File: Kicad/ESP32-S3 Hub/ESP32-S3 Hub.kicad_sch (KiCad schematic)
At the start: 26 parts, among them U1 ESP32-S3, Y1 ABM11-40.000MHZ-B1U-T3, 10ppm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

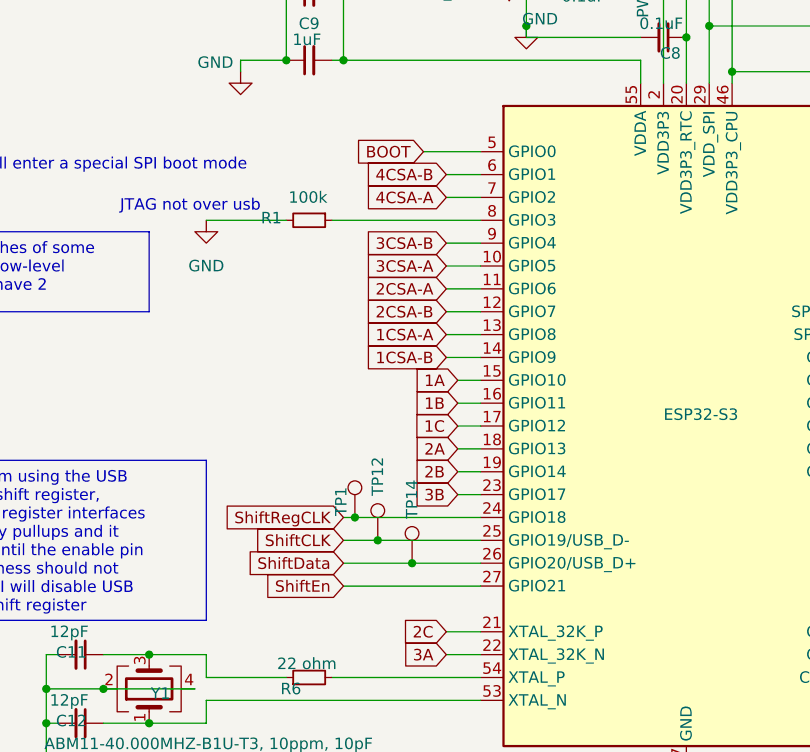
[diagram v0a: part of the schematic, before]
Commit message: Finished basic routing
Now I have to fix some things to try and reduce crosstalk, and improve signal integrity. The likelihood of me being able to completely fix it is low, due to limited space. I also have to run the DRC, and fix the silkscreen.
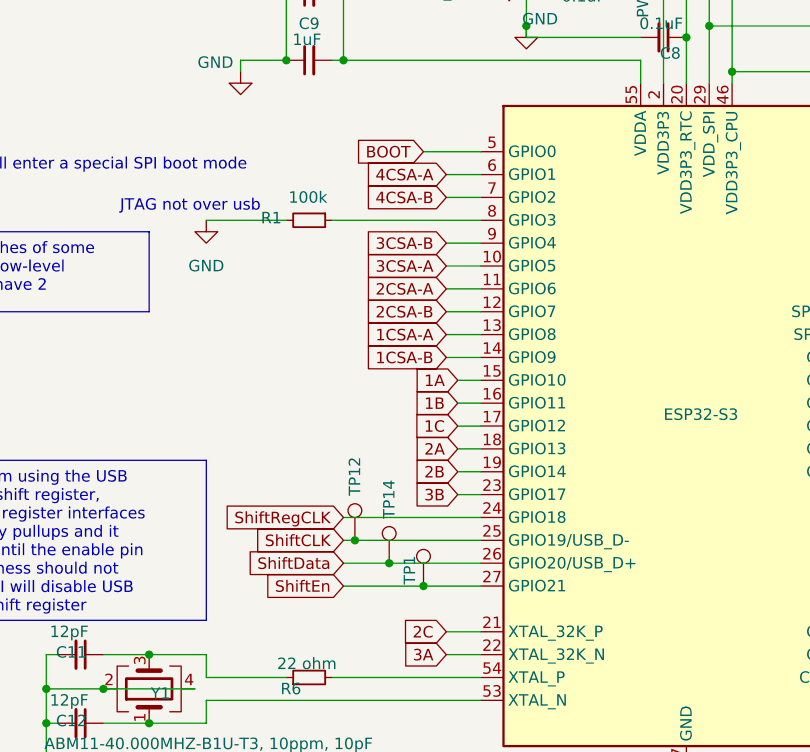
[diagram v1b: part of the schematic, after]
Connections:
- net 4CSA-A: now also U1.6 (GPIO1); no longer U1.7 (GPIO2)
- net 4CSA-B: now also U1.7 (GPIO2); no longer U1.6 (GPIO1)
- net ShiftEn: now also TP1.1
- net ShiftRegCLK: no longer TP1.1
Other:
- moved on the sheet: TP1, TP12, TP14
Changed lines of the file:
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@@
 	)
 	(junction
-		(at 110.49 105.41)
-		(diameter 0)
-		(color 0 0 0 0)
-	)
-	(junction
-		(at 107.95 102.87)
+		(at 111.76 107.95)
 		(diameter 0)
 		(color 0 0 0 0)
@@
 	)
 	(junction
+		(at 107.95 105.41)
+		(diameter 0)
+		(color 0 0 0 0)
+	)
+	(junction
 		(at 142.24 31.75)
 		(diameter 0)
@@
 	)
 	(junction
-		(at 114.3 107.95)
+		(at 115.57 110.49)
 		(diameter 0)
 		(color 0 0 0 0)
@@
 	(wire
 		(pts
-			(xy 107.95 102.87) (xy 121.92 102.87)
-		)
-		(stroke
-			(width 0)
-			(type default)
-		)
-	)
-	(wire
-		(pts
 			(xy 73.66 121.92) (xy 73.66 125.73)
 		)
@@
 	(wire
 		(pts
+			(xy 111.76 107.95) (xy 121.92 107.95)
+		)
+		(stroke
+			(width 0)
+			(type default)
+		)
+	)
+	(wire
+		(pts
 			(xy 176.53 102.87) (xy 180.34 102.87)
 		)
@@
 	(wire
 		(pts
-			(xy 106.68 102.87) (xy 107.95 102.87)
+			(xy 106.68 102.87) (xy 121.92 102.87)
 		)
 		(stroke
@@
 	(wire
 		(pts
-			(xy 110.49 105.41) (xy 121.92 105.41)
-		)
-		(stroke
-			(width 0)
-			(type default)
-		)
-	)
-	(wire
-		(pts
 			(xy 139.7 54.61) (xy 139.7 52.07)
 		)
@@
 	(wire
 		(pts
+			(xy 107.95 105.41) (xy 121.92 105.41)
+		)
+		(stroke
+			(width 0)
+			(type default)
+		)
+	)
+	(wire
+		(pts
 			(xy 85.09 118.11) (xy 91.44 118.11)
 		)
@@
 	(wire
 		(pts
-			(xy 106.68 110.49) (xy 121.92 110.49)
+			(xy 106.68 110.49) (xy 115.57 110.49)
 		)
 		(stroke
@@
 	(wire
 		(pts
-			(xy 106.68 107.95) (xy 114.3 107.95)
+			(xy 106.68 107.95) (xy 111.76 107.95)
 		)
 		(stroke
@@
 	(wire
 		(pts
-			(xy 142.24 40.64) (xy 142.24 44.45)
+			(xy 115.57 110.49) (xy 121.92 110.49)
 		)
 		(stroke
@@
 	(wire
 		(pts
-			(xy 137.16 40.64) (xy 142.24 40.64)
+			(xy 142.24 40.64) (xy 142.24 44.45)
 		)
 		(stroke
@@
 	(wire
 		(pts
-			(xy 118.11 85.09) (xy 121.92 85.09)
+			(xy 137.16 40.64) (xy 142.24 40.64)
 		)
 		(stroke
@@
 	(wire
 		(pts
-			(xy 91.44 125.73) (xy 85.09 125.73)
+			(xy 118.11 85.09) (xy 121.92 85.09)
 		)
 		(stroke
@@
 	(wire
 		(pts
-			(xy 114.3 107.95) (xy 121.92 107.95)
+			(xy 91.44 125.73) (xy 85.09 125.73)
 		)
 		(stroke
@@
 	(wire
 		(pts
-			(xy 106.68 105.41) (xy 110.49 105.41)
+			(xy 106.68 105.41) (xy 107.95 105.41)
 		)
 		(stroke
@@
 	(global_label "4CSA-B"
 		(shape input)
-		(at 118.11 64.77 180)
+		(at 118.11 67.31 180)
 		(fields_autoplaced yes)
 		(effects
@@
 		)
 		(property "Intersheetrefs" "${INTERSHEET_REFS}"
-			(at 107.5048 64.77 0)
+			(at 107.5048 67.31 0)
 			(effects
 				(font
@@
 	(global_label "4CSA-A"
 		(shape input)
-		(at 118.11 67.31 180)
+		(at 118.11 64.77 180)
 		(fields_autoplaced yes)
 		(effects
@@
 		)
 		(property "Intersheetrefs" "${INTERSHEET_REFS}"
-			(at 107.6862 67.31 0)
+			(at 107.6862 64.77 0)
 			(effects
 				(font
@@
 	(symbol
 		(lib_id "Connector:TestPoint")
-		(at 107.95 102.87 0)
+		(at 115.57 110.49 0)
 		(unit 1)
 		(exclude_from_sim no)
@@
 		(dnp no)
 		(property "Reference" "TP1"
-			(at 106.426 101.092 90)
+			(at 114.046 108.712 90)
 			(effects
 				(font
@@
 		)
 		(property "Value" "~"
-			(at 108.204 93.98 90)
+			(at 115.824 101.6 90)
 			(effects
 				(font
@@
 		)
 		(property "Footprint" "TestPoint:TestPoint_Pad_D1.0mm"
-			(at 113.03 102.87 0)
+			(at 120.65 110.49 0)
 			(effects
 				(font
@@
 		)
 		(property "Datasheet" "~"
-			(at 113.03 102.87 0)
+			(at 120.65 110.49 0)
 			(effects
 				(font
@@
 		)
 		(property "Description" "test point"
-			(at 107.95 102.87 0)
+			(at 115.57 110.49 0)
 			(effects
 				(font
@@
 	(symbol
 		(lib_id "Connector:TestPoint")
-		(at 114.3 107.95 0)
+		(at 111.76 107.95 0)
 		(unit 1)
 		(exclude_from_sim no)
@@
 		(dnp no)
 		(property "Reference" "TP14"
-			(at 114.3 100.838 90)
+			(at 111.76 100.838 90)
 			(effects
 				(font
@@
 		)
 		(property "Value" "~"
-			(at 114.554 99.06 90)
+			(at 112.014 99.06 90)
 			(effects
 				(font
@@
 		)
 		(property "Footprint" "TestPoint:TestPoint_Pad_D1.0mm"
-			(at 119.38 107.95 0)
+			(at 116.84 107.95 0)
 			(effects
 				(font
@@
 		)
 		(property "Datasheet" "~"
-			(at 119.38 107.95 0)
+			(at 116.84 107.95 0)
 			(effects
 				(font
@@
 		)
 		(property "Description" "test point"
-			(at 114.3 107.95 0)
+			(at 111.76 107.95 0)
 			(effects
 				(font
@@
 	(symbol
 		(lib_id "Connector:TestPoint")
-		(at 110.49 105.41 0)
+		(at 107.95 105.41 0)
 		(unit 1)
 		(exclude_from_sim no)
@@
 		(dnp no)
 		(property "Reference" "TP12"
-			(at 110.49 98.298 90)
+			(at 107.95 98.298 90)
 			(effects
 				(font
@@
 		)
 		(property "Value" "~"
-			(at 110.744 96.52 90)
+			(at 108.204 96.52 90)
 			(effects
 				(font
@@
 		)
 		(property "Footprint" "TestPoint:TestPoint_Pad_D1.0mm"
-			(at 115.57 105.41 0)
+			(at 113.03 105.41 0)
 			(effects
 				(font
@@
 		)
 		(property "Datasheet" "~"
-			(at 115.57 105.41 0)
+			(at 113.03 105.41 0)
 			(effects
 				(font
@@
 		)
 		(property "Description" "test point"
-			(at 110.49 105.41 0)
+			(at 107.95 105.41 0)
 			(effects
 				(font

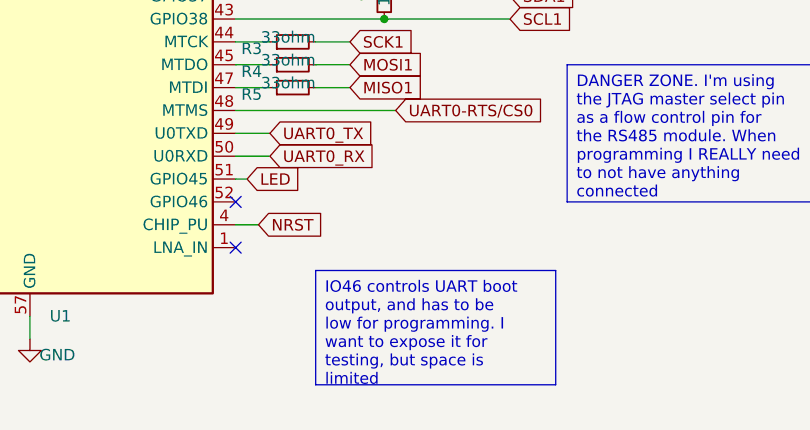
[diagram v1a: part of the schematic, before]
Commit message: Cleaned up wires, added IO46 testpad, added license to design files
I also added a ground plane to In3.
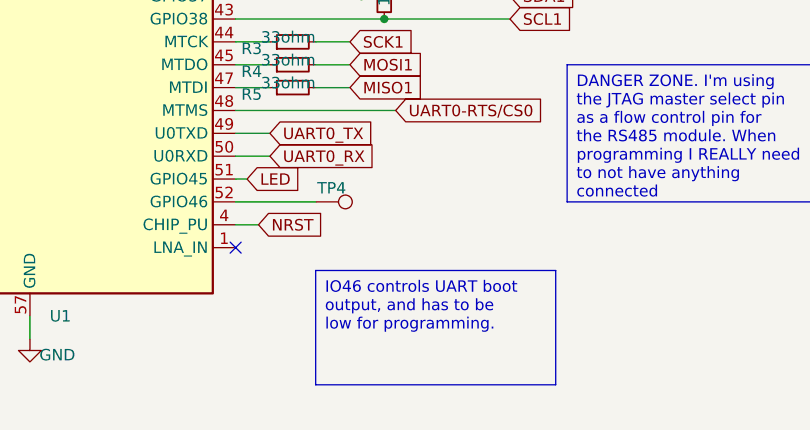
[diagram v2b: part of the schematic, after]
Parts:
- added TP4: ~, TestPoint:TestPoint_Pad_D1.0mm, symbol Connector:TestPoint
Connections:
- net at U1.52 (GPIO46): now also TP4.1
- no-connect marks 9 -> 8
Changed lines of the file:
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@@
 		(title "CACKLE -  Hub")
 		(date "2024-10-08")
+		(rev "V1")
+		(comment 1 "Licensed under CERN-OHL-S v2")
+		(comment 2 "Author: Asher Edwards")
 	)
 	(junction
@@
 		(diameter 0)
 		(color 0 0 0 0)
-	)
-	(no_connect
-		(at 167.64 118.11)
 	)
 	(no_connect
@@
 		(pts
 			(xy 106.68 44.45) (xy 106.68 43.18)
+		)
+		(stroke
+			(width 0)
+			(type default)
+		)
+	)
+	(wire
+		(pts
+			(xy 176.53 118.11) (xy 167.64 118.11)
 		)
 		(stroke
@@
 		)
 	)
-	(text_box "IO46 controls UART boot output, and has to be low for programming. I want to expose it for testing, but space is limited"
+	(text_box "IO46 controls UART boot output, and has to be low for programming."
 		(exclude_from_sim no)
 		(at 176.53 125.73 0)
@@
 			)
 		)
+	)
+	(symbol
+		(lib_id "Connector:TestPoint")
+		(at 176.53 118.11 270)
+		(unit 1)
+		(exclude_from_sim no)
+		(in_bom no)
+		(on_board yes)
+		(dnp no)
+		(property "Reference" "TP4"
+			(at 178.308 116.586 90)
+			(effects
+				(font
+					(size 1.27 1.27)
+				)
+			)
+		)
+		(property "Value" "~"
+			(at 185.42 118.364 90)
+			(effects
+				(font
+					(size 1.27 1.27)
+				)
+			)
+		)
+		(property "Footprint" "TestPoint:TestPoint_Pad_D1.0mm"
+			(at 176.53 123.19 0)
+			(effects
+				(font
+					(size 1.27 1.27)
+				)
+				(hide yes)
+			)
+		)
+		(property "Datasheet" "~"
+			(at 176.53 123.19 0)
+			(effects
+				(font
+					(size 1.27 1.27)
+				)
+				(hide yes)
+			)
+		)
+		(property "Description" "test point"
+			(at 176.53 118.11 0)
+			(effects
+				(font
+					(size 1.27 1.27)
+				)
+				(hide yes)
+			)
+		)
+		(pin "1"
+		)
+		(instances
+			(project "ESP32-S3 Hub"
+				(path "/a8c80fba-3bca-4358-b5bb-9ebf9383c658"
+					(reference "TP4")
+					(unit 1)
+				)
+			)
+		)

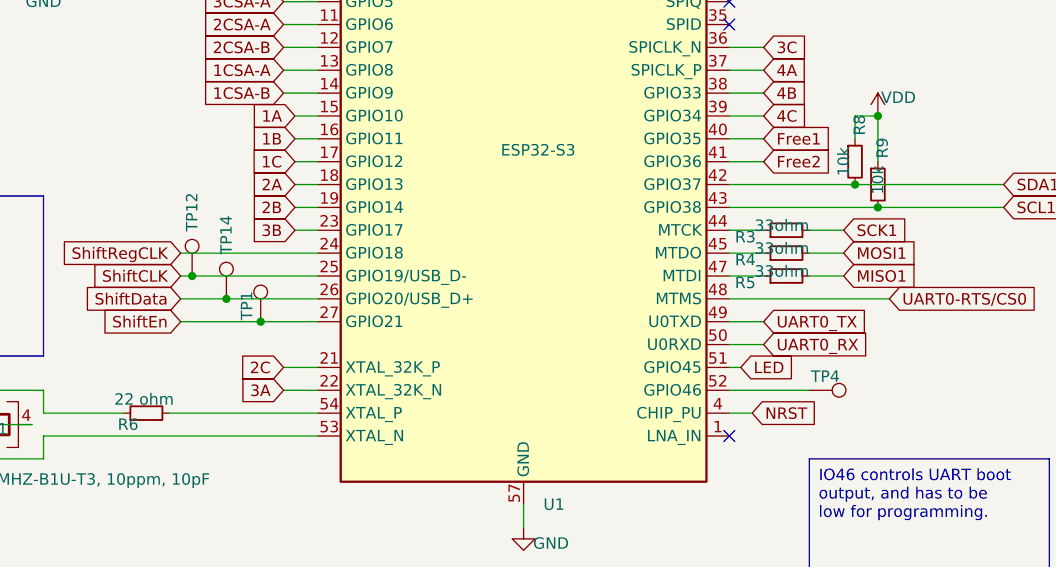
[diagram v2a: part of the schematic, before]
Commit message: Arranged Silkscreen
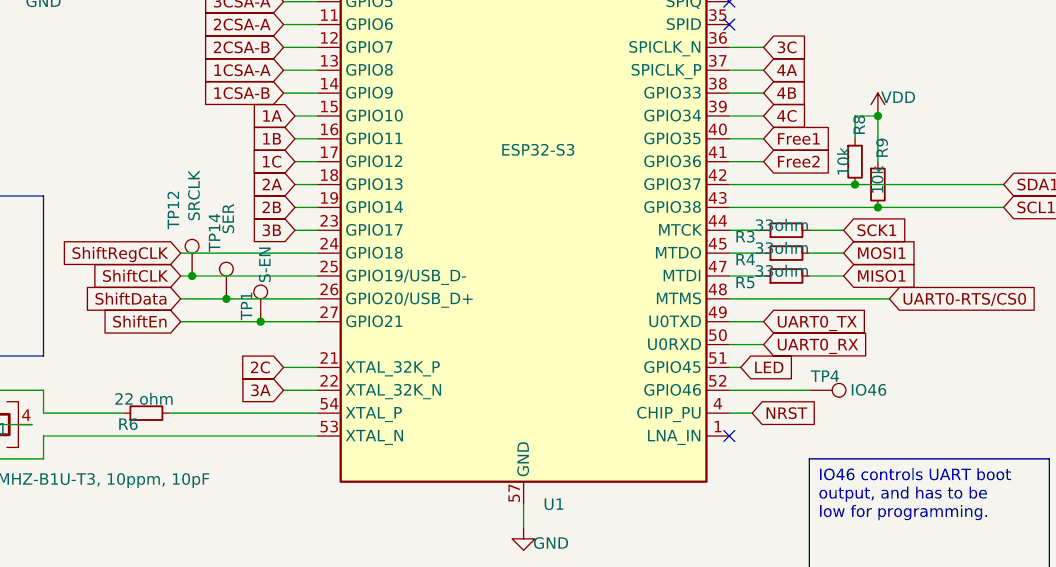
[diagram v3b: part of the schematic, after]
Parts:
- TP1: value ~ -> S-EN
- TP12: value ~ -> SRCLK
- TP14: value ~ -> SER
- TP4: value ~ -> IO46
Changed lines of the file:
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@@
 			)
 		)
-		(property "Value" "~"
-			(at 185.42 118.364 90)
+		(property "Value" "IO46"
+			(at 183.134 118.11 90)
 			(effects
 				(font
@@
 			)
 		)
-		(property "Value" "~"
-			(at 115.824 101.6 90)
+		(property "Value" "S-EN"
+			(at 116.078 104.14 90)
 			(effects
 				(font
@@
 		(dnp no)
 		(property "Reference" "TP14"
-			(at 111.76 100.838 90)
-			(effects
-				(font
-					(size 1.27 1.27)
-				)
-			)
-		)
-		(property "Value" "~"
+			(at 110.49 100.584 90)
+			(effects
+				(font
+					(size 1.27 1.27)
+				)
+			)
+		)
+		(property "Value" "SER"
 			(at 112.014 99.06 90)
 			(effects
@@
 		(dnp no)
 		(property "Reference" "TP12"
-			(at 107.95 98.298 90)
-			(effects
-				(font
-					(size 1.27 1.27)
-				)
-			)
-		)
-		(property "Value" "~"
+			(at 105.918 98.044 90)
+			(effects
+				(font
+					(size 1.27 1.27)
+				)
+			)
+		)
+		(property "Value" "SRCLK"
 			(at 108.204 96.52 90)
 			(effects

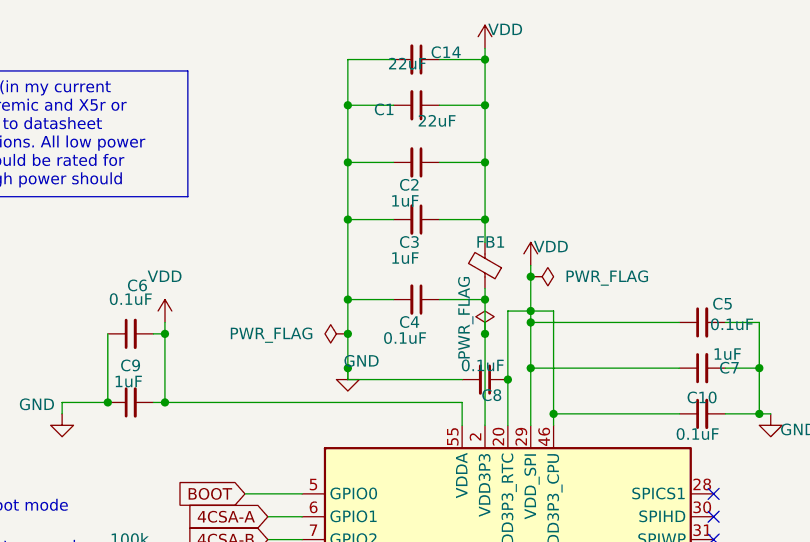
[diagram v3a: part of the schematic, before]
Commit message: Fixed OE pin by adding pullup, updated silkscreen
The silkscreen looks really nice now, I have all the port labels.
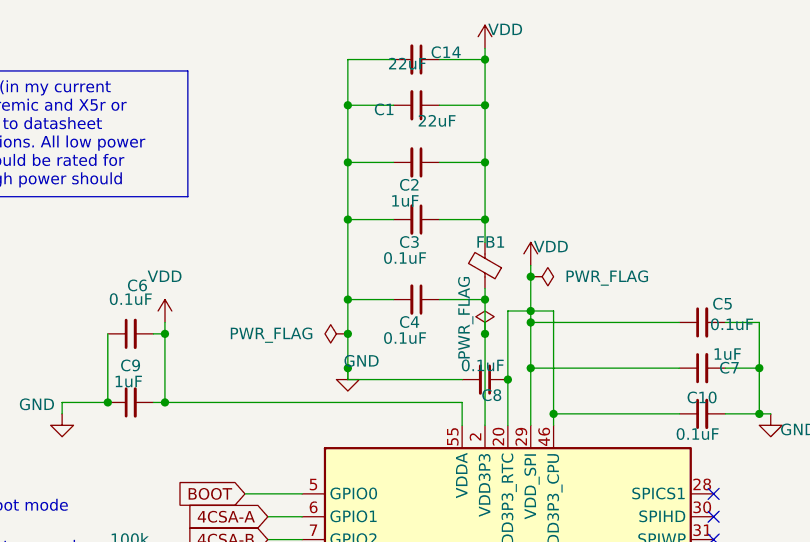
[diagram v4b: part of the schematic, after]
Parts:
- C3: value 1uF -> 0.1uF
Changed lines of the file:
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@@
 			)
 		)
-		(property "Value" "1uF"
+		(property "Value" "0.1uF"
 			(at 133.35 36.068 90)
 			(effects

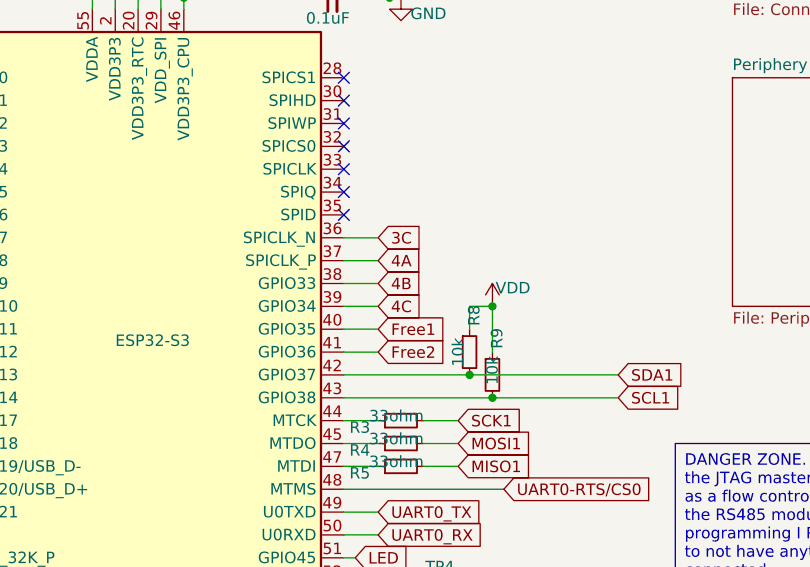
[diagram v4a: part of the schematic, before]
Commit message: Fixed left side swapped headers, tuned RS485 skew
The left side shouldn't have been mirrored, it should be rotated 180. I had to swap the CSA and the PWM output headers, which was a hassle. I also tuned the RS485 trace skews finally, something I forgot when I "finished" the board a month ago.
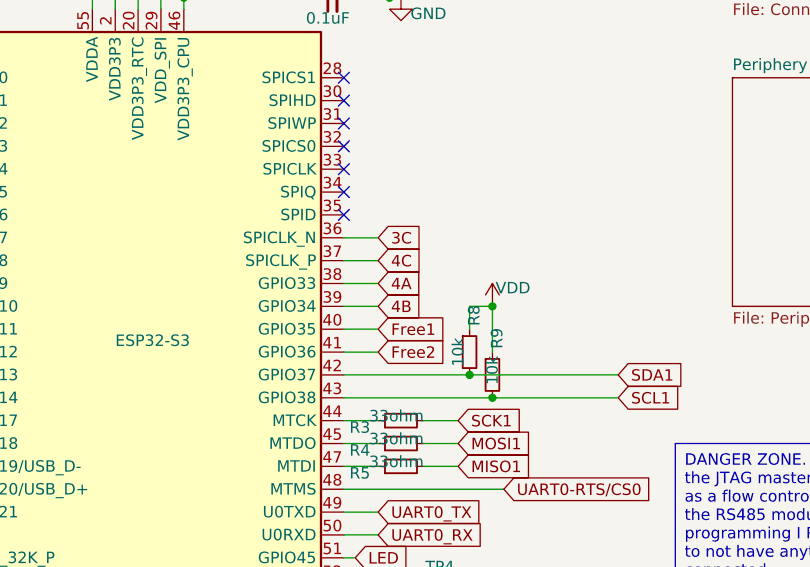
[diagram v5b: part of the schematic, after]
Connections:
- net 4A: now also U1.38 (GPIO33); no longer U1.37 (SPICLK_P)
- net 4B: now also U1.39 (GPIO34); no longer U1.38 (GPIO33)
- net 4C: now also U1.37 (SPICLK_P); no longer U1.39 (GPIO34)
